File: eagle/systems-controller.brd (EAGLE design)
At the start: 80 x 40 mm, 52 parts, among them IC1 MK20DX256VLH7, IC2 MKL02Z32VFG4, IC3 TPS6214XRGT, J1 SIG, J2 PWR, J3 GND, Q1 FA-238, Q2 PMV20ENR, Q3 PMV20ENR, Q4 PMV20ENR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

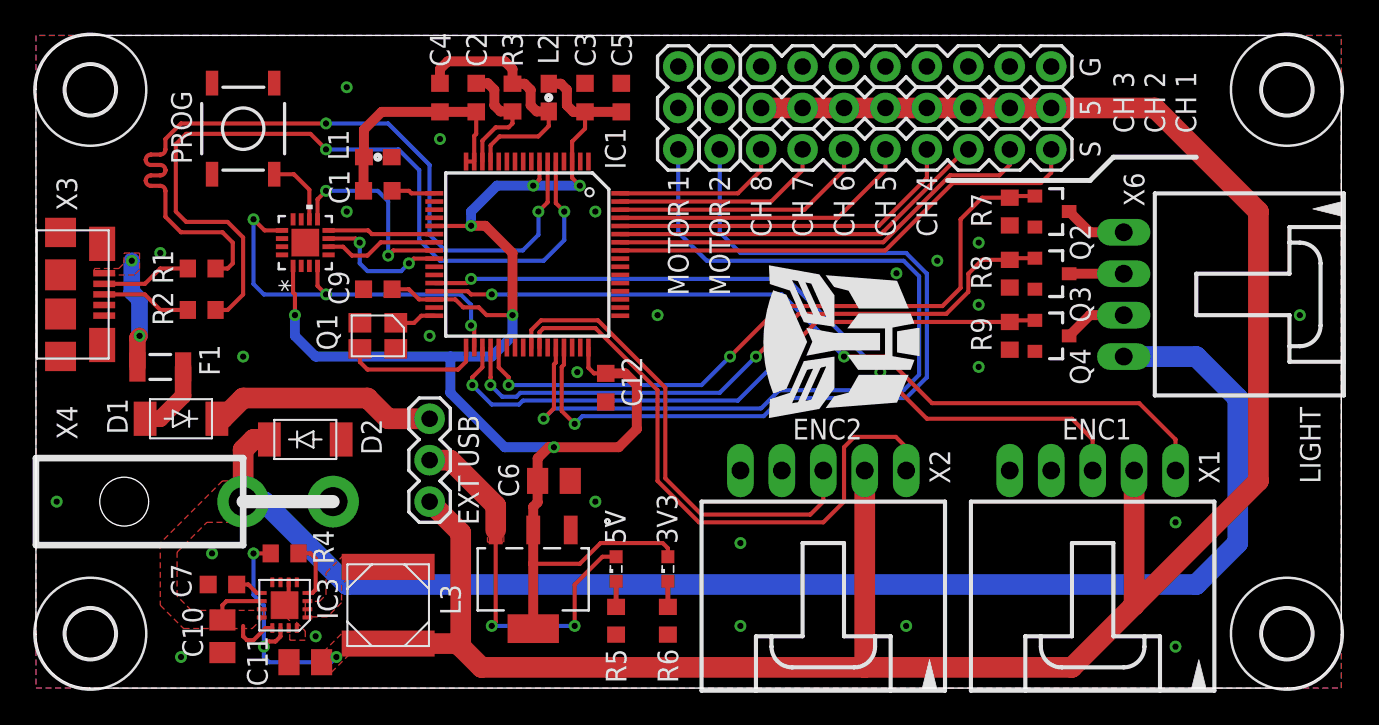
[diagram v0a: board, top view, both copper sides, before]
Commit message: fixed reversed encoder connectors
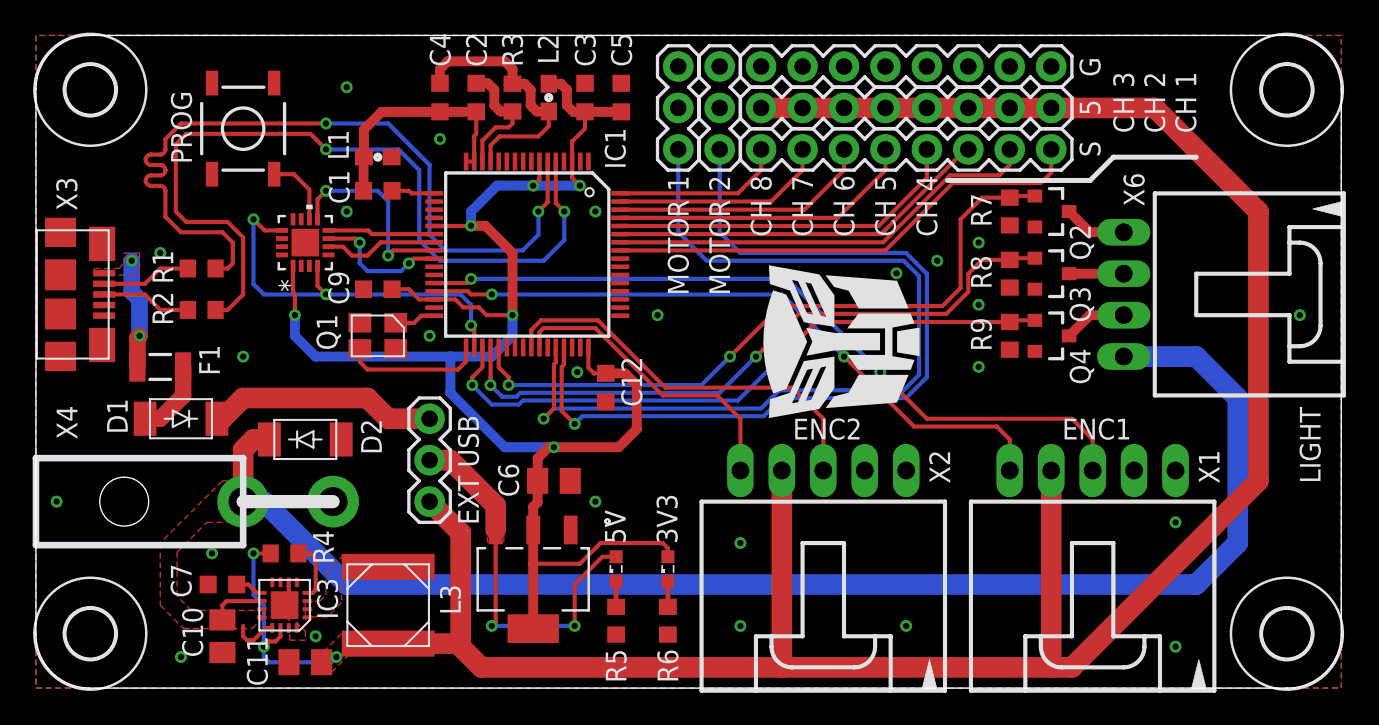
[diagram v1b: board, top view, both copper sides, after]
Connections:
- net +5V: now also X1.4, X2.4; no longer X1.2, X2.2
- net ENC1B: now also X1.5; no longer X1.1
- net ENC2B: now also X2.5; no longer X2.1
- net GND: now also X1.1, X2.1; no longer X1.5, X2.5
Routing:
- net ENC2B: track 37.5 -> 18.8 mm
- net ENC1B: track 51.1 -> 40.9 mm
- net ENC2A: track 29.6 -> 24.9 mm
- net +5V: track 152.5 -> 156.3 mm
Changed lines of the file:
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@@
 <contactref element="J3" pad="2"/>
 <contactref element="J3" pad="1"/>
-<contactref element="X2" pad="5"/>
-<contactref element="X1" pad="5"/>
 <contactref element="Q2" pad="2"/>
 <contactref element="R7" pad="1"/>
@@
 <contactref element="J5" pad="1"/>
 <via x="52.745640625" y="25.4254" extent="1-16" drill="0.381"/>
+<contactref element="X1" pad="1"/>
+<contactref element="X2" pad="1"/>
 </signal>
 <signal name="N$17">
@@
 <contactref element="J2" pad="7"/>
 <contactref element="J2" pad="8"/>
-<contactref element="X1" pad="2"/>
-<contactref element="X2" pad="2"/>
 <polygon width="0.254" layer="1" thermals="no">
 <vertex x="16.98625" y="0.9525"/>
@@
 <wire x1="26.035" y1="2.54" x2="26.035" y2="9.525" width="1.27" layer="1"/>
 <wire x1="26.035" y1="9.525" x2="24.13" y2="11.43" width="1.27" layer="1"/>
-<wire x1="67.31" y1="13.335" x2="67.31" y2="5.08" width="1.27" layer="1"/>
-<wire x1="67.31" y1="5.08" x2="63.5" y2="1.27" width="1.27" layer="1"/>
-<wire x1="63.5" y1="1.27" x2="50.8" y2="1.27" width="1.27" layer="1"/>
-<wire x1="50.8" y1="1.27" x2="27.305" y2="1.27" width="1.27" layer="1"/>
+<wire x1="63.5" y1="1.27" x2="62.23" y2="1.27" width="1.27" layer="1"/>
+<wire x1="62.23" y1="1.27" x2="45.72" y2="1.27" width="1.27" layer="1"/>
+<wire x1="45.72" y1="1.27" x2="27.305" y2="1.27" width="1.27" layer="1"/>
 <wire x1="27.305" y1="1.27" x2="26.035" y2="2.54" width="1.27" layer="1"/>
 <wire x1="21.59" y1="2.73" x2="25.845" y2="2.73" width="1.27" layer="1"/>
 <wire x1="25.845" y1="2.73" x2="26.035" y2="2.54" width="1.27" layer="1"/>
-<wire x1="50.8" y1="13.335" x2="50.8" y2="1.27" width="1.27" layer="1"/>
 <wire x1="44.45" y1="35.56" x2="46.99" y2="35.56" width="1.27" layer="1"/>
 <wire x1="46.99" y1="35.56" x2="49.53" y2="35.56" width="1.27" layer="1"/>
@@
 <wire x1="68.58" y1="35.56" x2="74.93" y2="29.21" width="1.27" layer="1"/>
 <wire x1="74.93" y1="29.21" x2="74.93" y2="12.7" width="1.27" layer="1"/>
-<wire x1="74.93" y1="12.7" x2="67.31" y2="5.08" width="1.27" layer="1"/>
+<wire x1="74.93" y1="12.7" x2="63.5" y2="1.27" width="1.27" layer="1"/>
 <wire x1="68.58" y1="35.56" x2="62.23" y2="35.56" width="1.27" layer="1"/>
+<contactref element="X1" pad="4"/>
+<contactref element="X2" pad="4"/>
+<wire x1="45.72" y1="13.335" x2="45.72" y2="1.27" width="1.27" layer="1"/>
+<wire x1="62.23" y1="13.335" x2="62.23" y2="1.27" width="1.27" layer="1"/>
 </signal>
 <signal name="5VSCLT">
@@
 <signal name="ENC1B">
 <contactref element="IC1" pad="29"/>
-<contactref element="X1" pad="1"/>
 <wire x1="24.415" y1="24.325" x2="26.475" y2="24.325" width="0.254" layer="1"/>
 <wire x1="26.475" y1="24.325" x2="26.67" y2="24.13" width="0.254" layer="1"/>
@@
 <wire x1="45.72" y1="24.13" x2="49.53" y2="20.32" width="0.254" layer="16"/>
 <via x="49.53" y="20.32" extent="1-16" drill="0.381"/>
-<wire x1="49.53" y1="20.32" x2="52.07" y2="20.32" width="0.254" layer="1"/>
-<wire x1="52.07" y1="20.32" x2="54.9275" y2="17.4625" width="0.254" layer="1"/>
-<wire x1="54.9275" y1="17.4625" x2="67.6275" y2="17.4625" width="0.254" layer="1"/>
-<wire x1="67.6275" y1="17.4625" x2="69.85" y2="15.24" width="0.254" layer="1"/>
-<wire x1="69.85" y1="15.24" x2="69.85" y2="13.335" width="0.254" layer="1"/>
+<contactref element="X1" pad="5"/>
+<wire x1="49.53" y1="20.32" x2="53.81625" y2="16.03375" width="0.254" layer="1"/>
+<wire x1="53.81625" y1="16.03375" x2="58.89625" y2="16.03375" width="0.254" layer="1"/>
+<wire x1="58.89625" y1="16.03375" x2="59.69" y2="15.24" width="0.254" layer="1"/>
+<wire x1="59.69" y1="15.24" x2="59.69" y2="13.335" width="0.254" layer="1"/>
 </signal>
 <signal name="ENC1A">
 <contactref element="IC1" pad="28"/>
-<contactref element="X1" pad="3"/>
 <wire x1="24.415" y1="24.825" x2="26.4125" y2="24.825" width="0.254" layer="1"/>
 <wire x1="26.4125" y1="24.825" x2="26.67" y2="25.0825" width="0.254" layer="1"/>
@@
 <wire x1="51.7525" y1="19.3675" x2="54.61" y2="16.51" width="0.254" layer="1"/>
 <wire x1="54.61" y1="16.51" x2="63.5" y2="16.51" width="0.254" layer="1"/>
+<contactref element="X1" pad="3"/>
 <wire x1="63.5" y1="16.51" x2="64.77" y2="15.24" width="0.254" layer="1"/>
 <wire x1="64.77" y1="15.24" x2="64.77" y2="13.335" width="0.254" layer="1"/>
@@
 <signal name="ENC2B">
 <contactref element="IC1" pad="42"/>
-<contactref element="X2" pad="1"/>
 <wire x1="30.865" y1="20.875" x2="30.865" y2="21.81625" width="0.254" layer="1"/>
 <wire x1="30.865" y1="21.81625" x2="31.115" y2="22.06625" width="0.254" layer="1"/>
 <wire x1="31.115" y1="22.06625" x2="34.29" y2="22.06625" width="0.254" layer="1"/>
-<wire x1="34.29" y1="22.06625" x2="38.1" y2="18.25625" width="0.254" layer="1"/>
-<wire x1="38.1" y1="18.25625" x2="38.1" y2="12.7" width="0.254" layer="1"/>
-<wire x1="38.1" y1="12.7" x2="40.64" y2="10.16" width="0.254" layer="1"/>
-<wire x1="40.64" y1="10.16" x2="48.26" y2="10.16" width="0.254" layer="1"/>
-<wire x1="48.26" y1="10.16" x2="49.53" y2="11.43" width="0.254" layer="1"/>
-<wire x1="49.53" y1="11.43" x2="49.53" y2="14.76375" width="0.254" layer="1"/>
-<wire x1="49.53" y1="14.76375" x2="50.165" y2="15.39875" width="0.254" layer="1"/>
-<wire x1="50.165" y1="15.39875" x2="52.705" y2="15.39875" width="0.254" layer="1"/>
-<wire x1="52.705" y1="15.39875" x2="53.34" y2="14.76375" width="0.254" layer="1"/>
-<wire x1="53.34" y1="14.76375" x2="53.34" y2="13.335" width="0.254" layer="1"/>
+<wire x1="34.29" y1="22.06625" x2="38.4175" y2="17.93875" width="0.254" layer="1"/>
+<contactref element="X2" pad="5"/>
+<wire x1="38.4175" y1="17.93875" x2="41.75125" y2="17.93875" width="0.254" layer="1"/>
+<wire x1="41.75125" y1="17.93875" x2="43.18" y2="16.51" width="0.254" layer="1"/>
+<wire x1="43.18" y1="16.51" x2="43.18" y2="13.335" width="0.254" layer="1"/>
 </signal>
 <signal name="ENC2A">
 <contactref element="IC1" pad="41"/>
-<contactref element="X2" pad="3"/>
 <wire x1="30.365" y1="20.875" x2="30.365" y2="21.95125" width="0.254" layer="1"/>
 <wire x1="30.365" y1="21.95125" x2="30.95625" y2="22.5425" width="0.254" layer="1"/>
 <wire x1="30.95625" y1="22.5425" x2="34.44875" y2="22.5425" width="0.254" layer="1"/>
 <wire x1="34.44875" y1="22.5425" x2="38.57625" y2="18.415" width="0.254" layer="1"/>
-<wire x1="38.57625" y1="12.85875" x2="38.57625" y2="18.415" width="0.254" layer="1"/>
-<wire x1="38.57625" y1="12.85875" x2="40.79875" y2="10.63625" width="0.254" layer="1"/>
-<wire x1="40.79875" y1="10.63625" x2="47.46625" y2="10.63625" width="0.254" layer="1"/>
-<wire x1="47.46625" y1="10.63625" x2="48.26" y2="11.43" width="0.254" layer="1"/>
-<wire x1="48.26" y1="11.43" x2="48.26" y2="13.335" width="0.254" layer="1"/>
+<contactref element="X2" pad="3"/>
+<wire x1="38.57625" y1="18.415" x2="46.355" y2="18.415" width="0.254" layer="1"/>
+<wire x1="46.355" y1="18.415" x2="48.26" y2="16.51" width="0.254" layer="1"/>
+<wire x1="48.26" y1="16.51" x2="48.26" y2="13.335" width="0.254" layer="1"/>
 </signal>
 <signal name="PWM1">
